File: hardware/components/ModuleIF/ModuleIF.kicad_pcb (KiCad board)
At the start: 2 copper layers, 12 parts, among them J101 Jumper, J102 Conn_01x04_MountingPin, U101 TCK106AF, U102 INA226

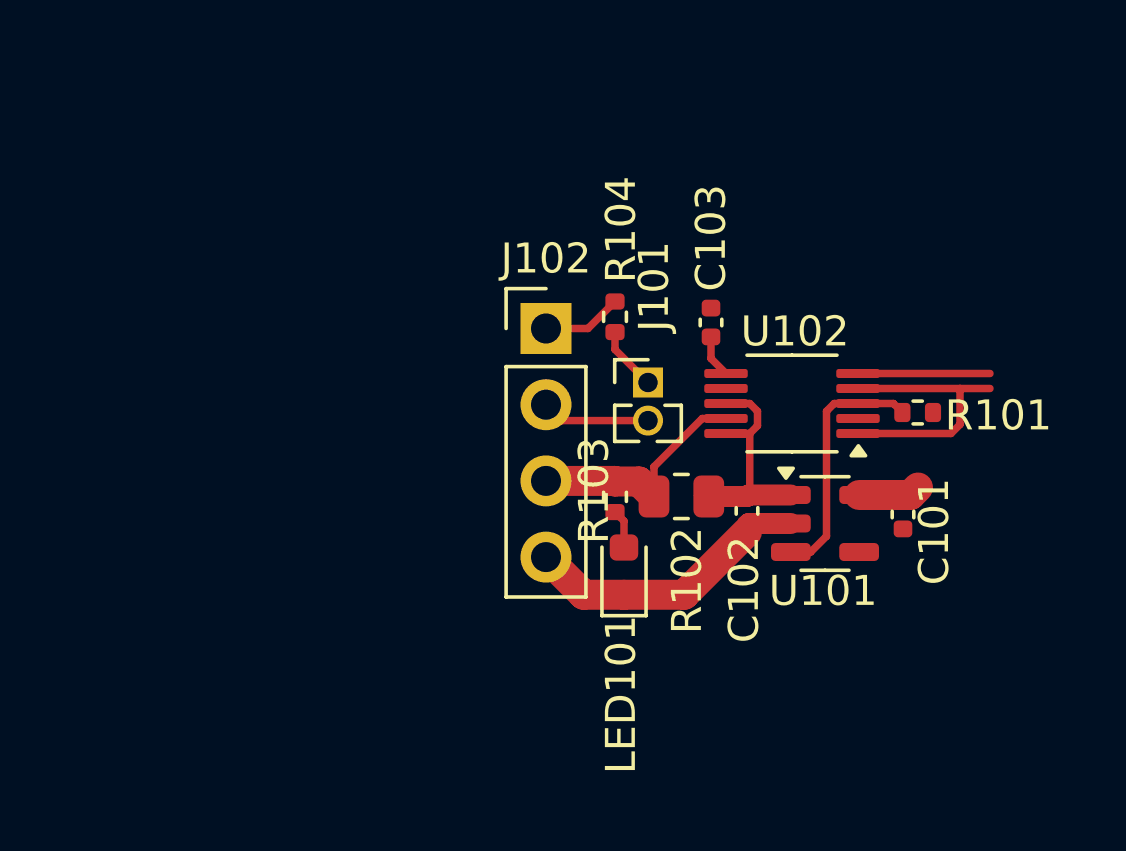
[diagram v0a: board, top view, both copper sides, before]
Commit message: SMAコネクタ・ロードスイッチ、groveコネクタについて修正しました
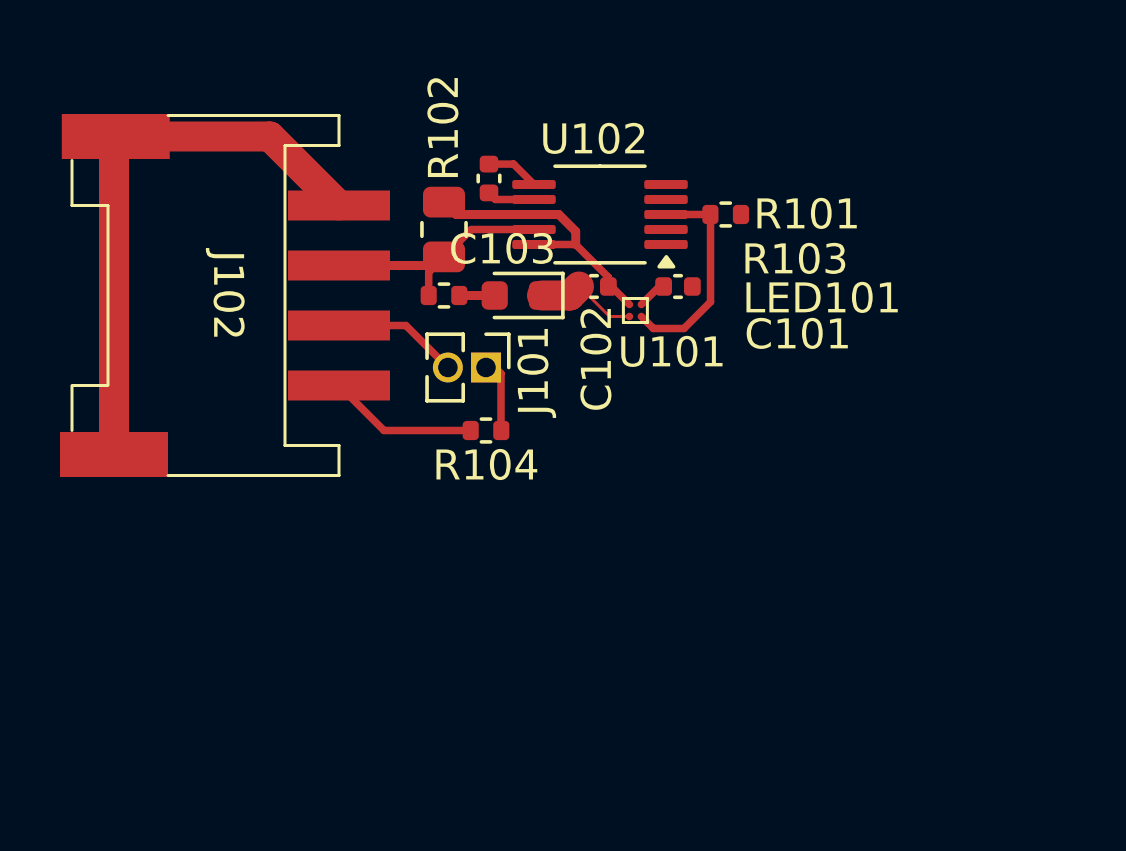
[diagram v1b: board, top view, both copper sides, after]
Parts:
- J102: footprint Connector_PinHeader_2.54mm:PinHeader_1x04_P2.54mm_Vertical -> WOBCLibrary:Grove_4P_L_SMD
- U101: footprint Package_TO_SOT_SMD:SOT-23-5 -> WOBCLibrary:WCSPD-4(0.8x0.8)
- moved R102 11.9 mm to (141.0, 91.0), turned to -90 degrees
- moved C101 10.7 mm to (148.8, 92.9), turned to 180 degrees
- moved J102 10.7 mm to (133.8, 93.2), turned to -90 degrees
- moved LED101 9.84 mm to (143.5, 93.2), turned to 180 degrees
- moved U101 9.51 mm to (147.4, 93.7), turned to -90 degrees
- moved R101 9.19 mm to (150.4, 90.5)
- moved C102 9.05 mm to (146.0, 92.9), turned to 0 degrees
- moved U102 8.98 mm to (146.2, 90.5)
- moved C103 8.82 mm to (142.5, 89.3), turned to 90 degrees
- moved R103 8.80 mm to (141.0, 93.2), turned to 180 degrees
- moved R104 5.73 mm to (142.4, 97.7), turned to 180 degrees
- moved J101 5.42 mm to (142.4, 95.6), turned to -90 degrees
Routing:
- net GND: track 9.57 -> 24.0 mm
- net /I2C_SDA: track 9.12 -> 0.00 mm
- net /I2C_SCL: track 4.40 -> 0.00 mm
- net /CANH: track 2.67 -> 5.01 mm
- net Net-(U101-VOUT): track 7.57 -> 9.61 mm
- net Net-(J102-Pin_3): track 7.87 -> 9.15 mm
- net Net-(U101-CONTROL): track 8.33 -> 7.16 mm
- net /VIN: track 2.07 -> 0.92 mm
- net /CANL: track 3.62 -> 4.21 mm
